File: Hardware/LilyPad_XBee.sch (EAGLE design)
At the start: 38 parts, among them U1 XBEE-1B3, U2 V_REG_LDOSMD

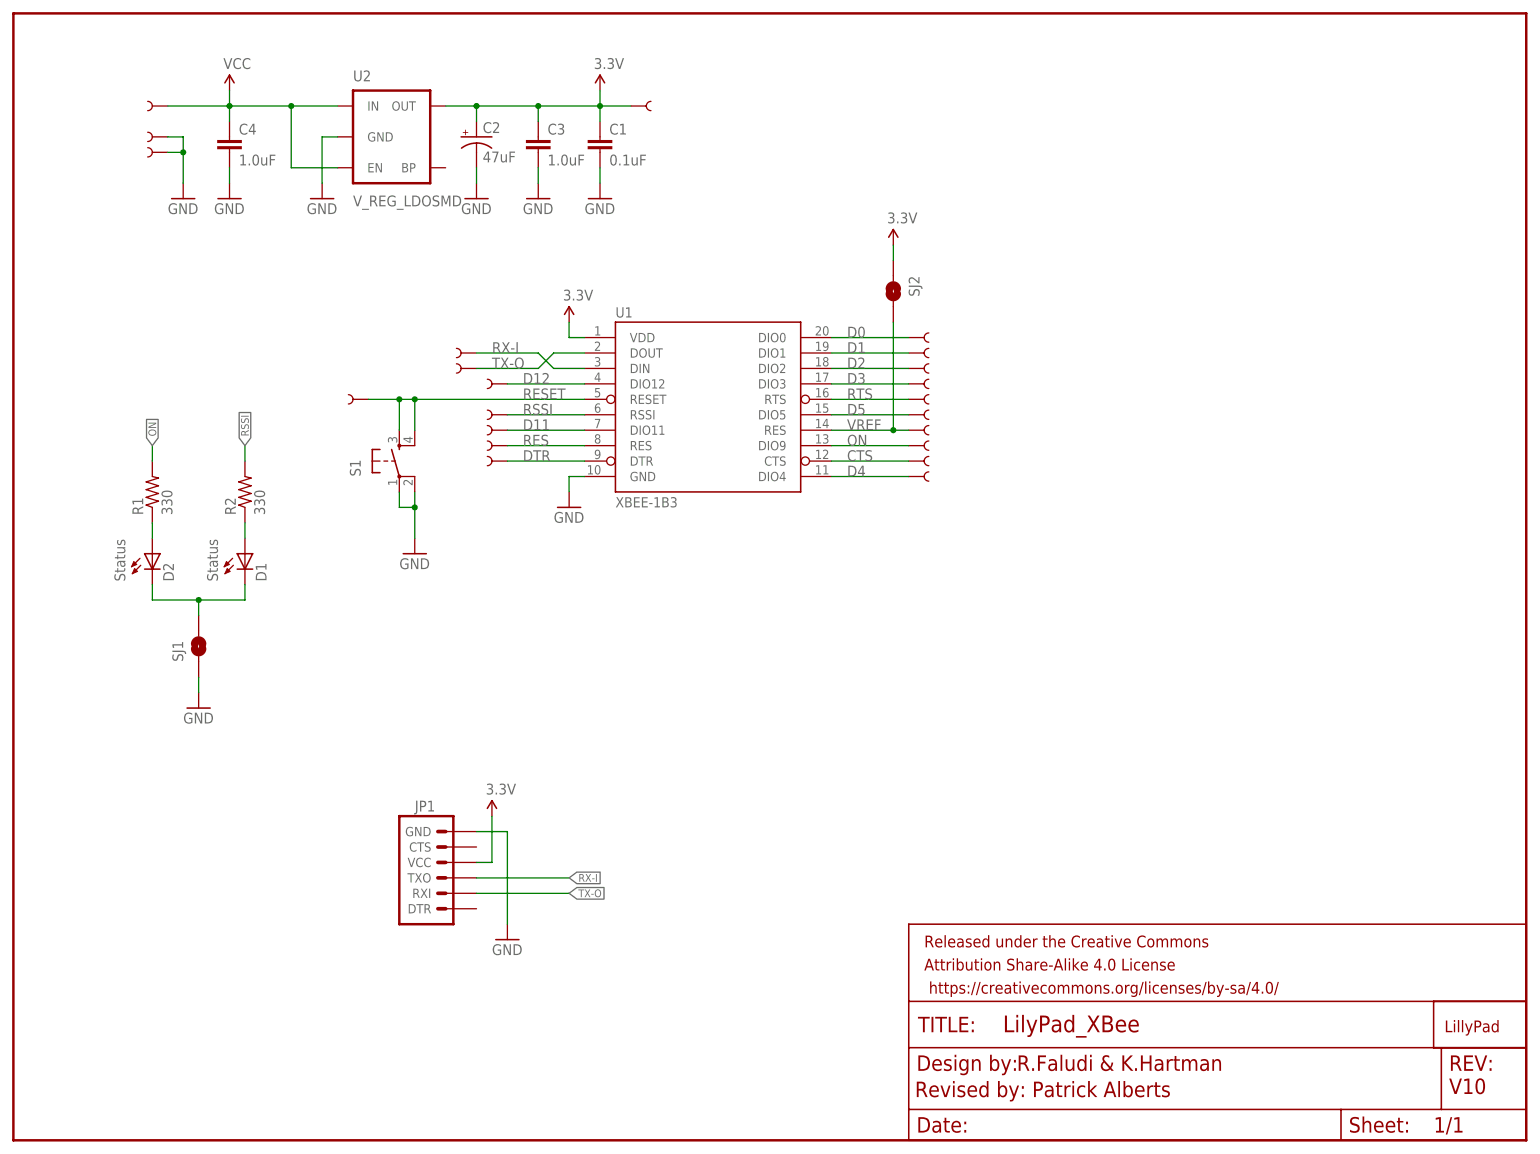
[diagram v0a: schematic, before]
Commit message: Added Silk / re arranged  LED Resistors
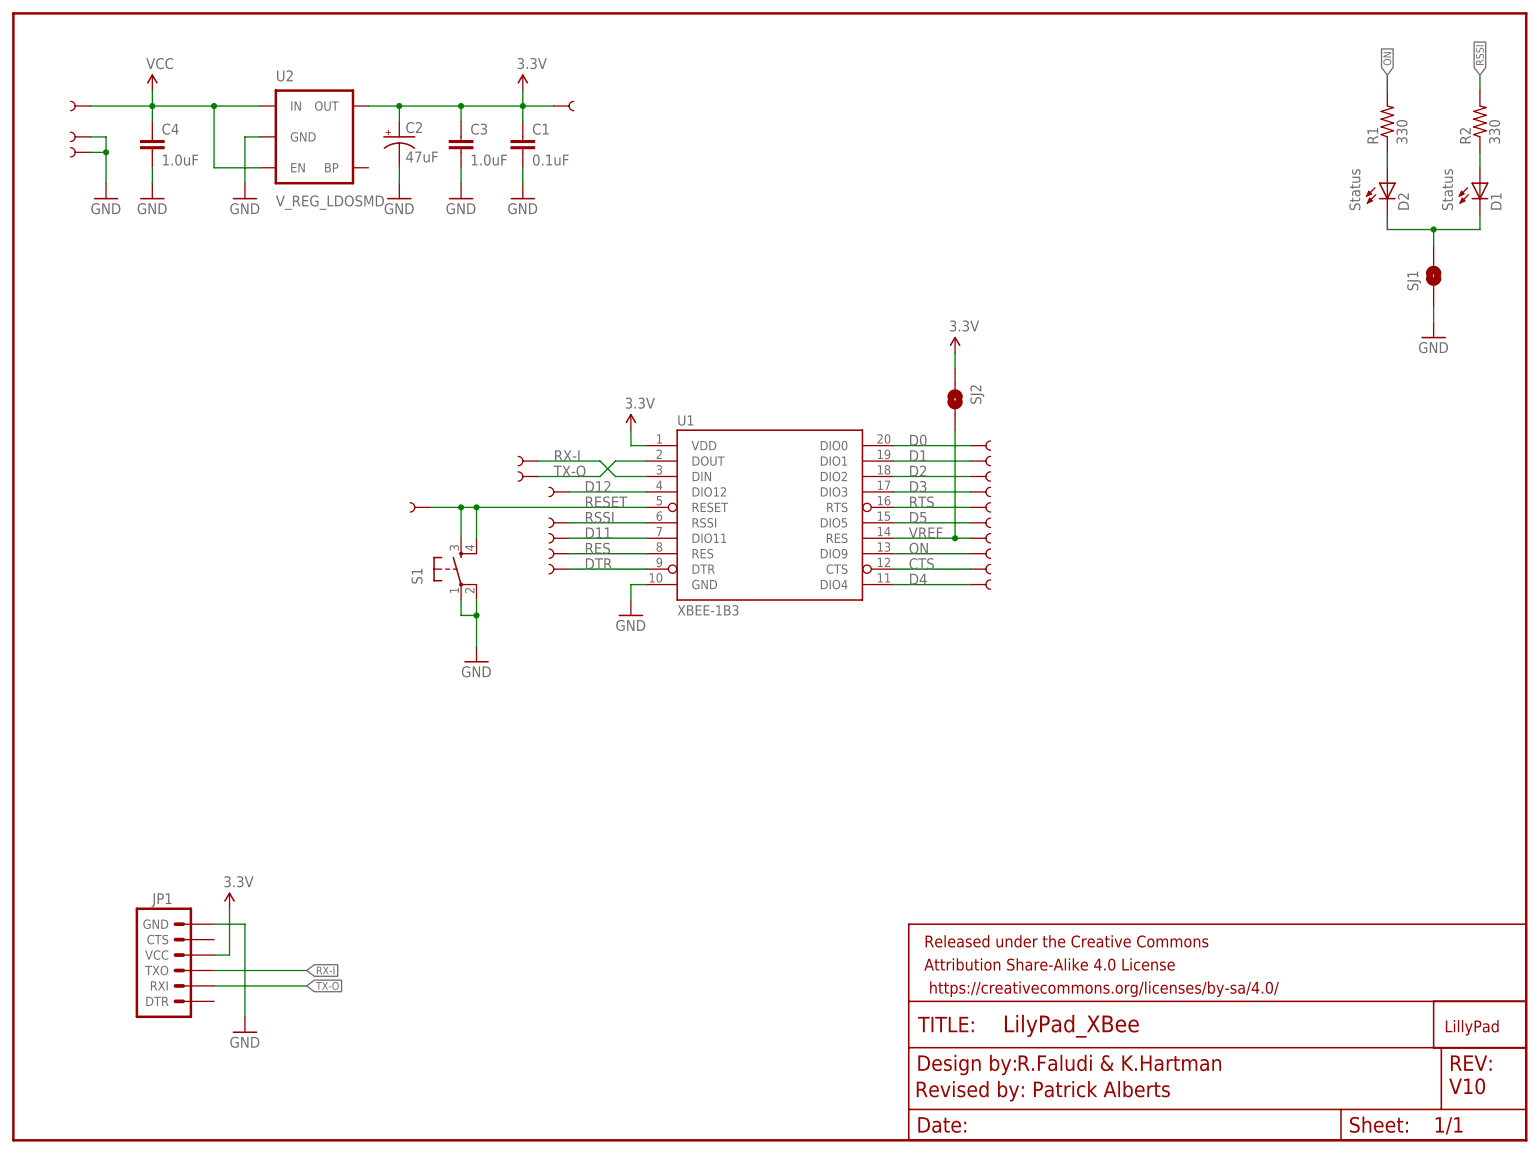
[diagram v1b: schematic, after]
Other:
- moved on the sheet: C1, C2, C3, C4, D1, D2, JP1, R1, R2, S1, SJ1, SJ2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

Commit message: Added Copper Flame/ Silk for jumper
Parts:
- added LOGO1: SFE_LOGO_FLAME.1COP, SparkFun-Aesthetics:SFE_LOGO_FLAME.1COP
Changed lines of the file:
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@@
 <part name="S1" library="SparkFun-Electromechanical" deviceset="TAC_SWITCH" device="SMD"/>
 <part name="GND5" library="SparkFun" deviceset="GND" device=""/>
+<part name="LOGO1" library="SparkFun-Aesthetics" deviceset="SFE_LOGO_FLAME" device=".1COP"/>
 </parts>
 <sheets>
@@
 <instance part="S1" gate="S" x="73.66" y="93.98" rot="R90"/>
 <instance part="GND5" gate="1" x="76.2" y="78.74"/>
+<instance part="LOGO1" gate="G$1" x="231.14" y="40.64"/>
 </instances>
 <busses>

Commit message: Added fiducials
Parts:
- added FID1, FID2: FIDUCIAL1X2, SparkFun-Aesthetics:FIDUCIAL1X2
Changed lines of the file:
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@@
 <?xml version="1.0" encoding="utf-8"?>
 <!DOCTYPE eagle SYSTEM "eagle.dtd">
-<eagle version="6.4">
+<eagle version="6.5.0">
 <drawing>
 <settings>
@@
 <part name="GND5" library="SparkFun" deviceset="GND" device=""/>
 <part name="LOGO1" library="SparkFun-Aesthetics" deviceset="SFE_LOGO_FLAME" device=".1COP"/>
+<part name="FID1" library="SparkFun-Aesthetics" deviceset="FIDUCIAL" device="1X2"/>
+<part name="FID2" library="SparkFun-Aesthetics" deviceset="FIDUCIAL" device="1X2"/>
 </parts>
 <sheets>
@@
 <instance part="GND5" gate="1" x="76.2" y="78.74"/>
 <instance part="LOGO1" gate="G$1" x="231.14" y="40.64"/>
+<instance part="FID1" gate="G$1" x="243.84" y="33.02"/>
+<instance part="FID2" gate="G$1" x="243.84" y="25.4"/>
 </instances>
 <busses>
